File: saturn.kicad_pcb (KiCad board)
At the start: 4 copper layers, 100 x 66 mm, 101 parts, among them J1 Conn_01x04_Pin, J10 Conn_01x04, J11 USB_B_Micro, J12 USB_C_Receptacle_USB2.0, J13 S3B-XH-A-1(LF)(SN), J14 Conn_01x04_Pin, J2 PMOD3_FULL, J3 Conn_01x06, J4 Conn_01x06, J6 Conn_01x10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

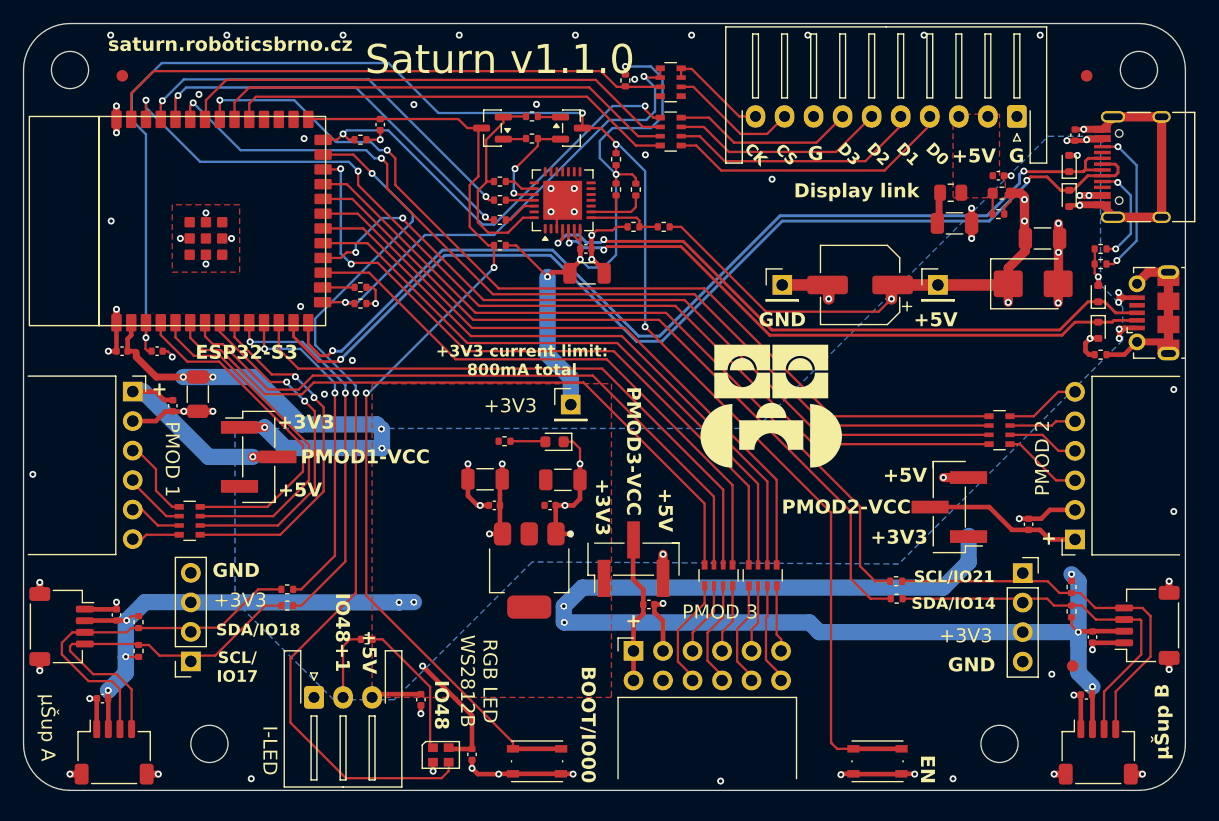
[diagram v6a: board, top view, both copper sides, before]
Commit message: Use SMT JST-XH connectors
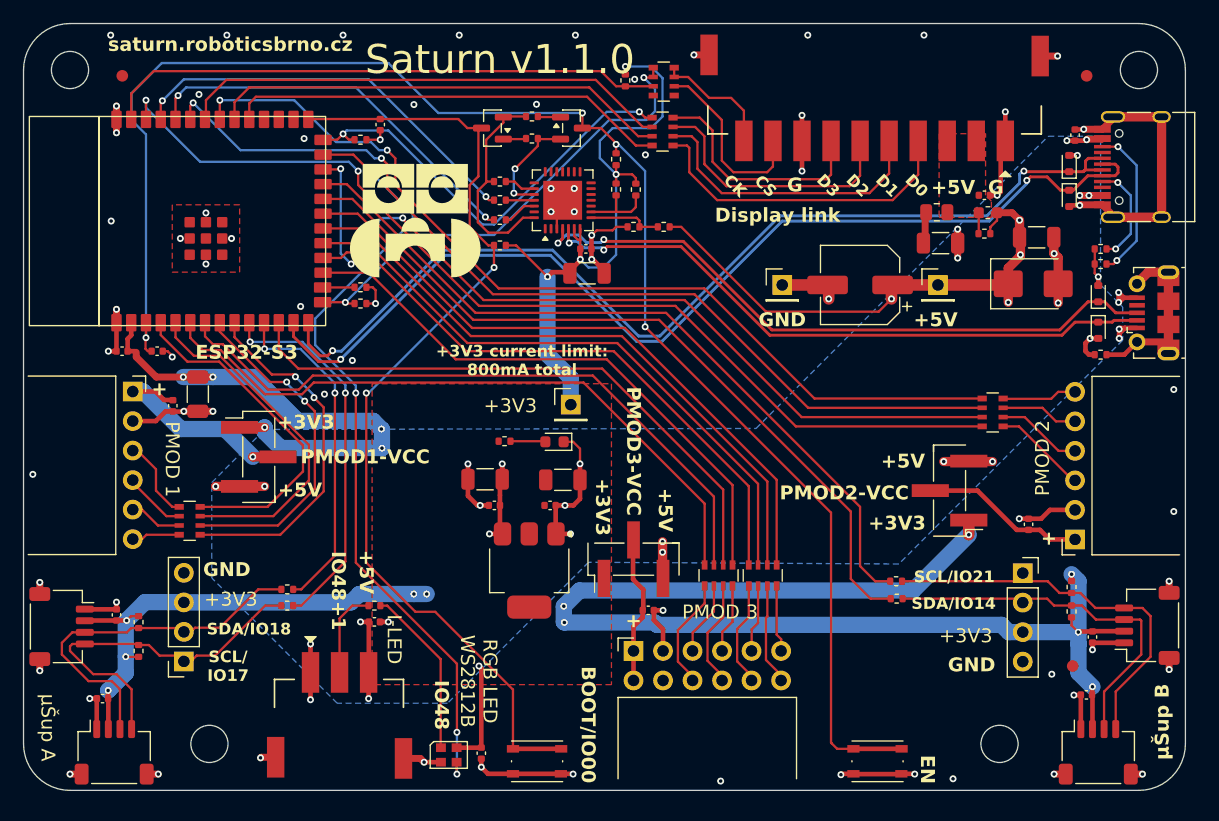
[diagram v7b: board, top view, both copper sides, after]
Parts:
- J13: value S3B-XH-A-1(LF)(SN) -> ZX-XH2.54-3PWT; footprint Connector_JST:JST_XH_S3B-XH-A-1_1x03_P2.50mm_Horizontal -> JST-XH-SMT:JST-XH-SMD-3Pin
- J6: value Conn_01x10 -> ZX-XH2.54-11PWT; footprint Connector_JST:JST_XH_S10B-XH-A-1_1x10_P2.50mm_Horizontal -> JST-XH-SMT:JST-XH-SMD-10Pin
- moved J6 12.5 mm to (118.2, 61.7)
- moved C10 7.80 mm to (75.2, 107.5), turned to 0 degrees
- moved R33 2.97 mm to (75.2, 106.1)
- moved J13 2.66 mm to (72.2, 115.5)
- moved C3 2.08 mm to (123.9, 74.9)
- moved C21 2.07 mm to (127.7, 70.8)
- moved FB1 2.07 mm to (128.0, 72.3)
- moved R3 2.07 mm to (123.6, 72.2)
- moved R9 2.07 mm to (127.7, 74.1)
- moved RN2 1.64 mm to (128.4, 89.5)
- moved JP3 1.42 mm to (124.7, 96.2)
- moved C16 0.81 mm to (84.4, 118.8)
- moved RN5 0.70 mm to (100.0, 65.3)
- moved U9 0.68 mm to (81.6, 119.0)
- moved RN6 0.60 mm to (100.1, 61.0)
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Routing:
- net GND: track 146.5 -> 167.8 mm, vias 86 -> 88
- net /SMART_LEDS: track 77.5 -> 67.6 mm, vias 2 -> 4
- net +5V: track 81.8 -> 89.8 mm, vias 15 -> 21
- net Net-(J6-Pin_9): track 11.2 -> 16.0 mm
- net Net-(J6-Pin_7): track 15.7 -> 20.4 mm
- net Net-(J6-Pin_6): track 18.6 -> 23.0 mm
- net Net-(J6-Pin_5): track 21.9 -> 25.5 mm
- net Net-(J6-Pin_4): track 24.7 -> 28.1 mm
- net Net-(U9-DOUT): track 11.9 -> 14.7 mm
- net Net-(J6-Pin_10): track 8.92 -> 10.6 mm
- net +3V3: track 247.0 -> 248.7 mm, vias 19 -> 20
- net /DISPLAY_IO3: track 39.0 -> 37.7 mm
- net Net-(J4-Pin_4): track 6.89 -> 8.11 mm
- net Net-(J4-Pin_3): track 6.17 -> 7.39 mm
- net /PMOD2_IO3: track 67.0 -> 65.7 mm
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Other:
- board text removed: "5V"

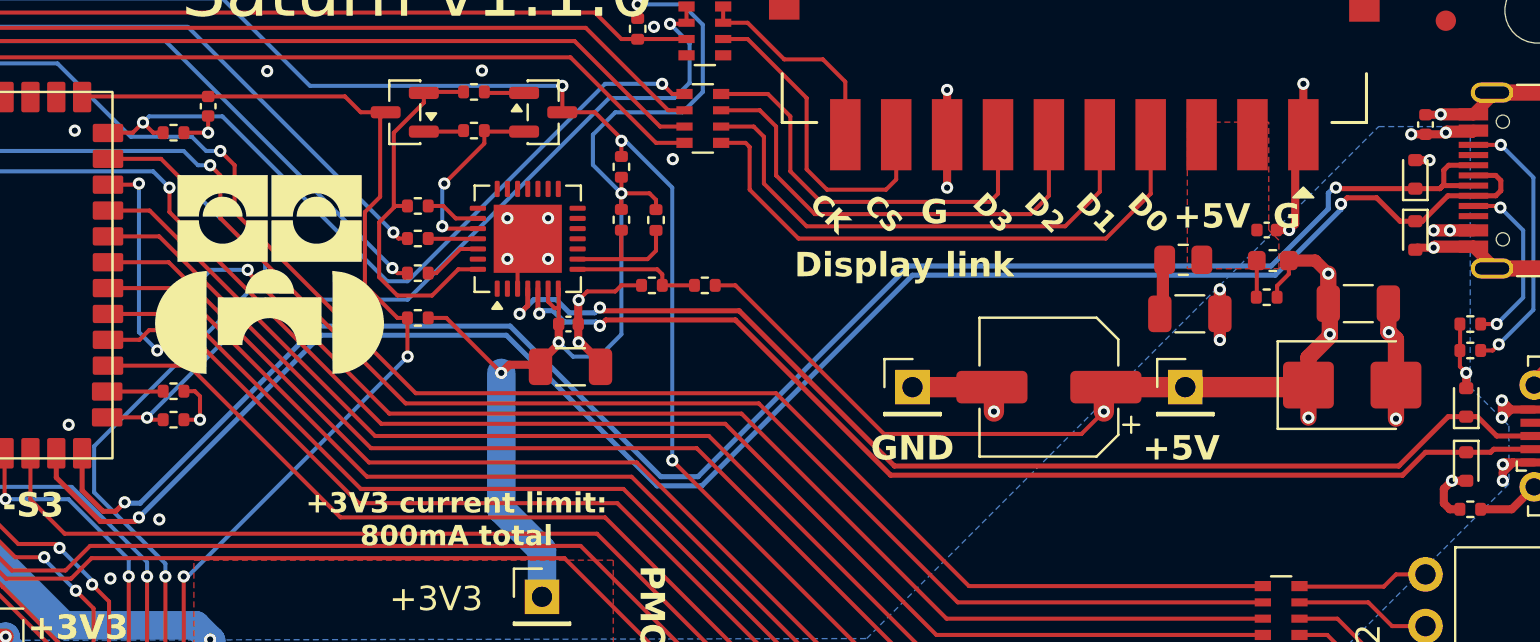
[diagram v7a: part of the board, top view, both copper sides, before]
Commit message: Tune silkscreen
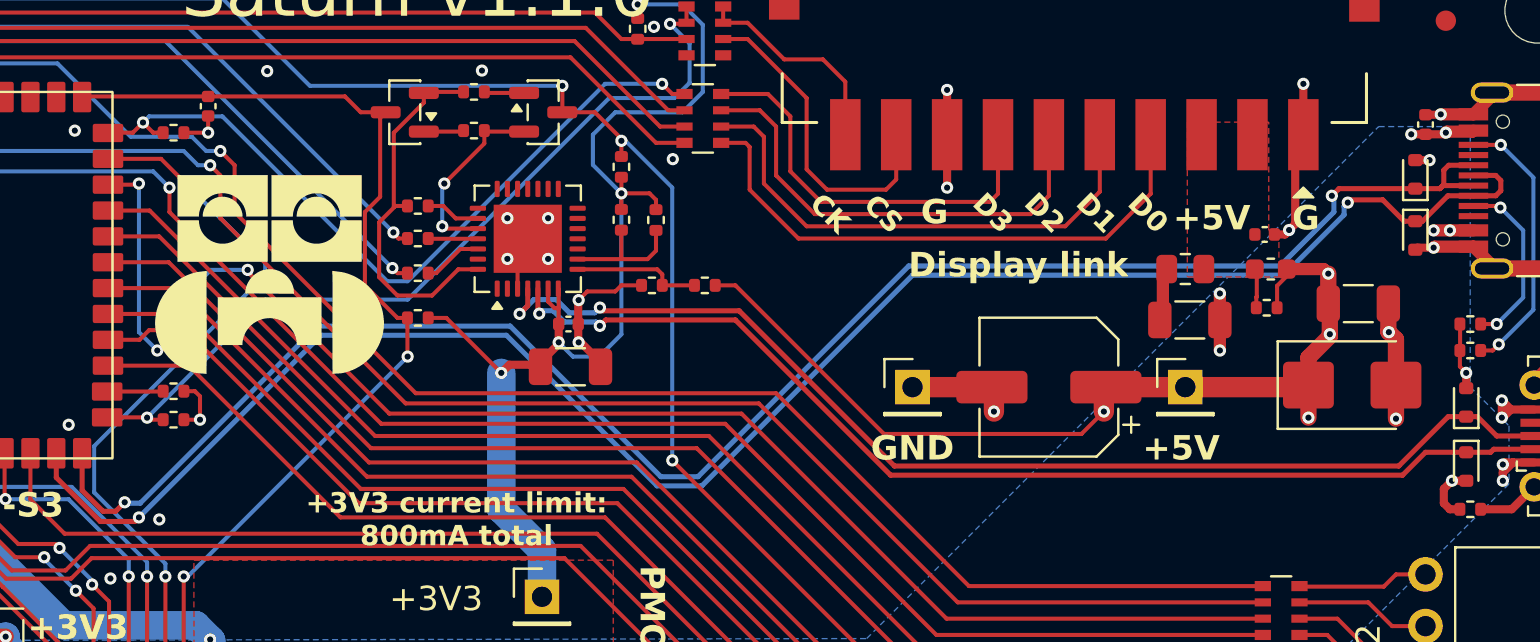
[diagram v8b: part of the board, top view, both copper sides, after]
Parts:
- J6: value ZX-XH2.54-11PWT -> ZX-XH2.54-10PWT
- moved R9 0.52 mm to (127.7, 74.6)
- moved R3 0.47 mm to (123.7, 72.7)
- moved FB1 0.43 mm to (127.9, 72.7)
- moved C3 0.30 mm to (123.9, 75.2)
- moved C21 0.24 mm to (127.6, 71.0)
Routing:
- net GND: track 167.8 -> 168.3 mm
